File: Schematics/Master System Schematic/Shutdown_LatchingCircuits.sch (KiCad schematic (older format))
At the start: 6 parts

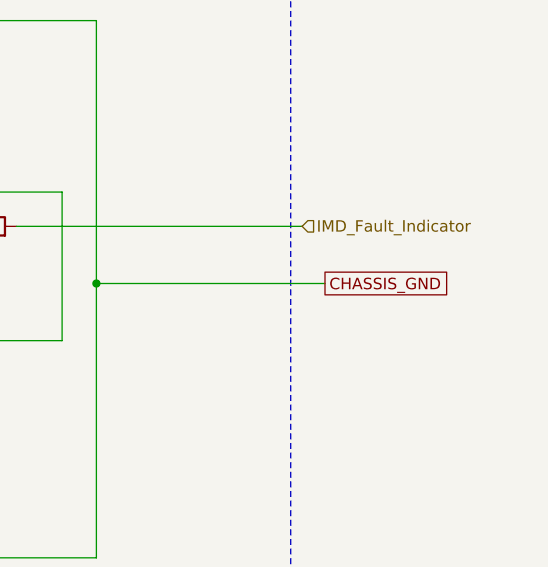
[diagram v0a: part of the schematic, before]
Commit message: Adding ground pin to fault pcb enclosure
Needed ground pin for fault pcb enclosure
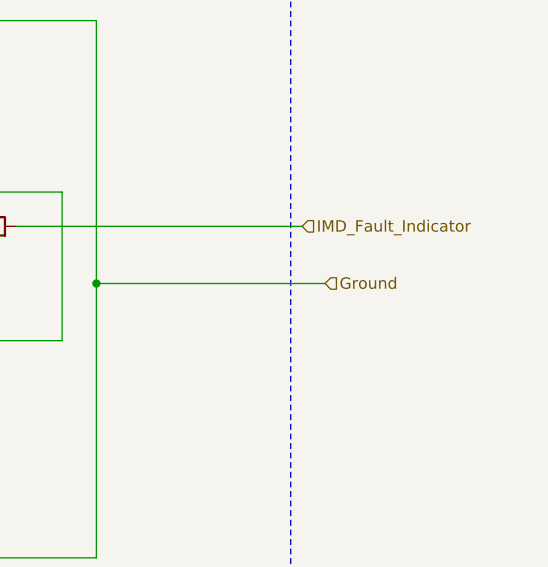
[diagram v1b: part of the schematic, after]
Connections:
- net labels added: Ground
- net labels removed: CHASSIS_GND
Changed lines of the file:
@@
 Text HLabel 6500 5550 2    50   Input ~ 0
 Shutdown_OUT
-Text GLabel 6600 3600 2    50   UnSpc ~ 0
-CHASSIS_GND
 Text HLabel 6500 3350 2    50   Input ~ 0
 IMD_Fault_Indicator
@@
 Wire Wire Line
 	5600 3600 6600 3600
+Text HLabel 6600 3600 2    50   Input ~ 0
+Ground
 $EndSCHEMATC

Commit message: Updated shutdown circuit to reflect changes
>updated latching circuit design to be 4 DPDT relays
>updated reset switch design to be dpst button to actuate both latches simultaneously
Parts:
- removed D? (x2): 1N4001, Diode_THT:D_DO-41_SOD81_P10.16mm_Horizontal, symbol Diode:1N4001
- removed K? (x2): 3PoleSwitchingRelay, symbol NER:3PoleSwitchingRelay
- removed R? (x2): 500, symbol Device:R
- added D? (x2): 1N4001, Diode_THT:D_DO-41_SOD81_P10.16mm_Horizontal, symbol Diode:1N4001
- added K? (x4): Omron DPDT Relay, Relay_THT:Relay_DPDT_Omron_G5V-2, symbol Relay:G5V-2
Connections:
- wire segments 50 -> 55
- no-connect marks 6 -> 12
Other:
- note removed: "Latching Fault Circuit PCB"

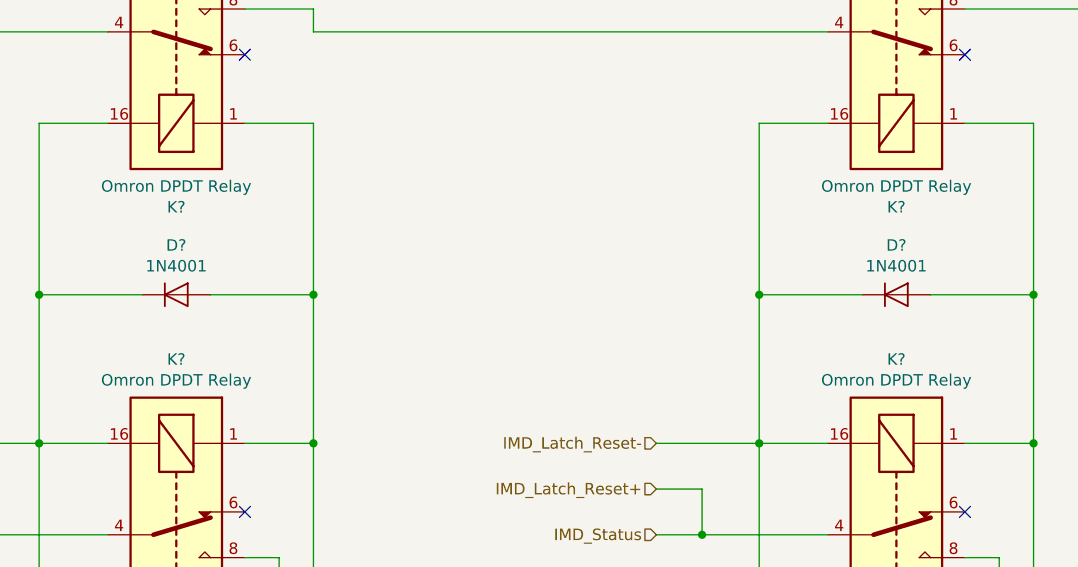
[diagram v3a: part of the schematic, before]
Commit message: Connectors and Start of Numbering
Created new generic connectors and applied numbering tool to whole project
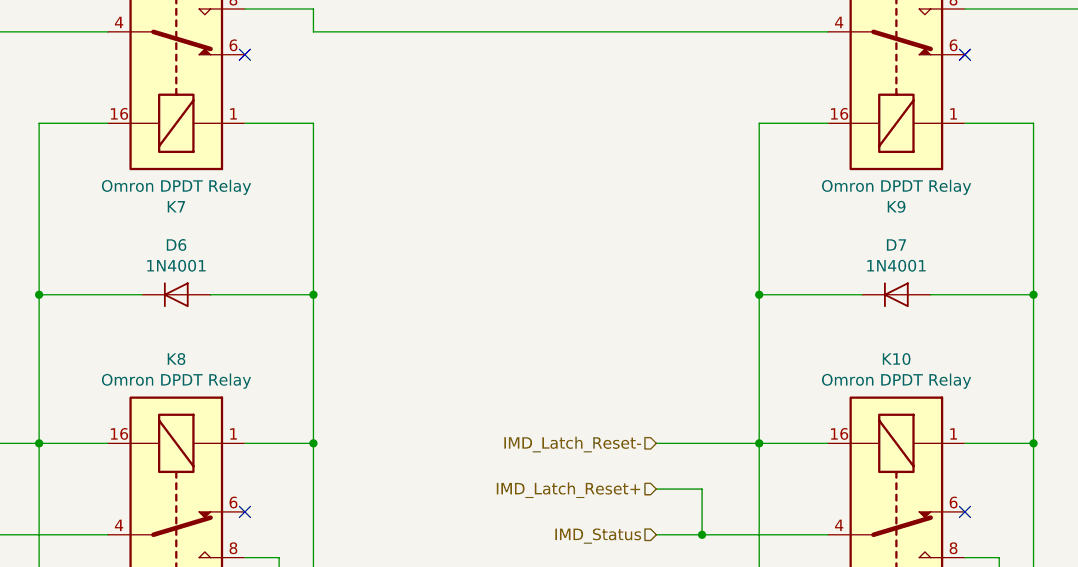
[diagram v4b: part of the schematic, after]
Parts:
- gave numbers to parts that had none: 6
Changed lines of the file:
@@
 EESchema Schematic File Version 4
+LIBS:Master System Schematic-cache
 EELAYER 30 0
 EELAYER END
@@
 Ground
 $Comp
-L Relay:G5V-2 K?
+L Relay:G5V-2 K10
 U 1 1 5F6E0AD1
 P 7350 4850
-F 0 "K?" V 6583 4850 50  0000 C CNN
+F 0 "K10" V 6583 4850 50  0000 C CNN
 F 1 "Omron DPDT Relay" V 6674 4850 50  0000 C CNN
 F 2 "Relay_THT:Relay_DPDT_Omron_G5V-2" H 8000 4800 50  0001 L CNN
@@
 $EndComp
 $Comp
-L Relay:G5V-2 K?
+L Relay:G5V-2 K9
 U 1 1 5F6E0AD7
 P 7350 2650
-F 0 "K?" V 6583 2650 50  0000 C CNN
+F 0 "K9" V 6583 2650 50  0000 C CNN
 F 1 "Omron DPDT Relay" V 6674 2650 50  0000 C CNN
 F 2 "Relay_THT:Relay_DPDT_Omron_G5V-2" H 8000 2600 50  0001 L CNN
@@
 $EndComp
 $Comp
-L Diode:1N4001 D?
+L Diode:1N4001 D7
 U 1 1 5F6E5F37
 P 7350 3800
-F 0 "D?" H 7350 4016 50  0000 C CNN
+F 0 "D7" H 7350 4016 50  0000 C CNN
 F 1 "1N4001" H 7350 3925 50  0000 C CNN
 F 2 "Diode_THT:D_DO-41_SOD81_P10.16mm_Horizontal" H 7350 3625 50  0001 C CNN
@@
 	3150 4650 3350 4650
 $Comp
-L Relay:G5V-2 K?
+L Relay:G5V-2 K8
 U 1 1 5F7C981B
 P 4200 4850
-F 0 "K?" V 3433 4850 50  0000 C CNN
+F 0 "K8" V 3433 4850 50  0000 C CNN
 F 1 "Omron DPDT Relay" V 3524 4850 50  0000 C CNN
 F 2 "Relay_THT:Relay_DPDT_Omron_G5V-2" H 4850 4800 50  0001 L CNN
@@
 $EndComp
 $Comp
-L Relay:G5V-2 K?
+L Relay:G5V-2 K7
 U 1 1 5F7C9821
 P 4200 2650
-F 0 "K?" V 3433 2650 50  0000 C CNN
+F 0 "K7" V 3433 2650 50  0000 C CNN
 F 1 "Omron DPDT Relay" V 3524 2650 50  0000 C CNN
 F 2 "Relay_THT:Relay_DPDT_Omron_G5V-2" H 4850 2600 50  0001 L CNN
@@
 $EndComp
 $Comp
-L Diode:1N4001 D?
+L Diode:1N4001 D6
 U 1 1 5F7C9827
 P 4200 3800
-F 0 "D?" H 4200 4016 50  0000 C CNN
+F 0 "D6" H 4200 4016 50  0000 C CNN
 F 1 "1N4001" H 4200 3925 50  0000 C CNN
 F 2 "Diode_THT:D_DO-41_SOD81_P10.16mm_Horizontal" H 4200 3625 50  0001 C CNN
